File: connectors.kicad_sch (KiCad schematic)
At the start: 21 parts, among them J10 Conn_01x02, J11 Conn_01x02, J12 Conn_01x02, J13 Conn_01x02, J14 Conn_01x02, J15 Conn_01x02, J16 Conn_01x02, J17 Conn_01x02, J18 Conn_01x02, J19 Conn_01x02, J2 Conn_01x02, J20 Conn_01x02, J21 Conn_01x02, J22 Conn_01x02, J23 Conn_01x02, J24 Conn_01x02, J3 Conn_01x02, J5 Conn_01x02, J7 Conn_01x02, J8 Conn_01x02, J9 Conn_01x02

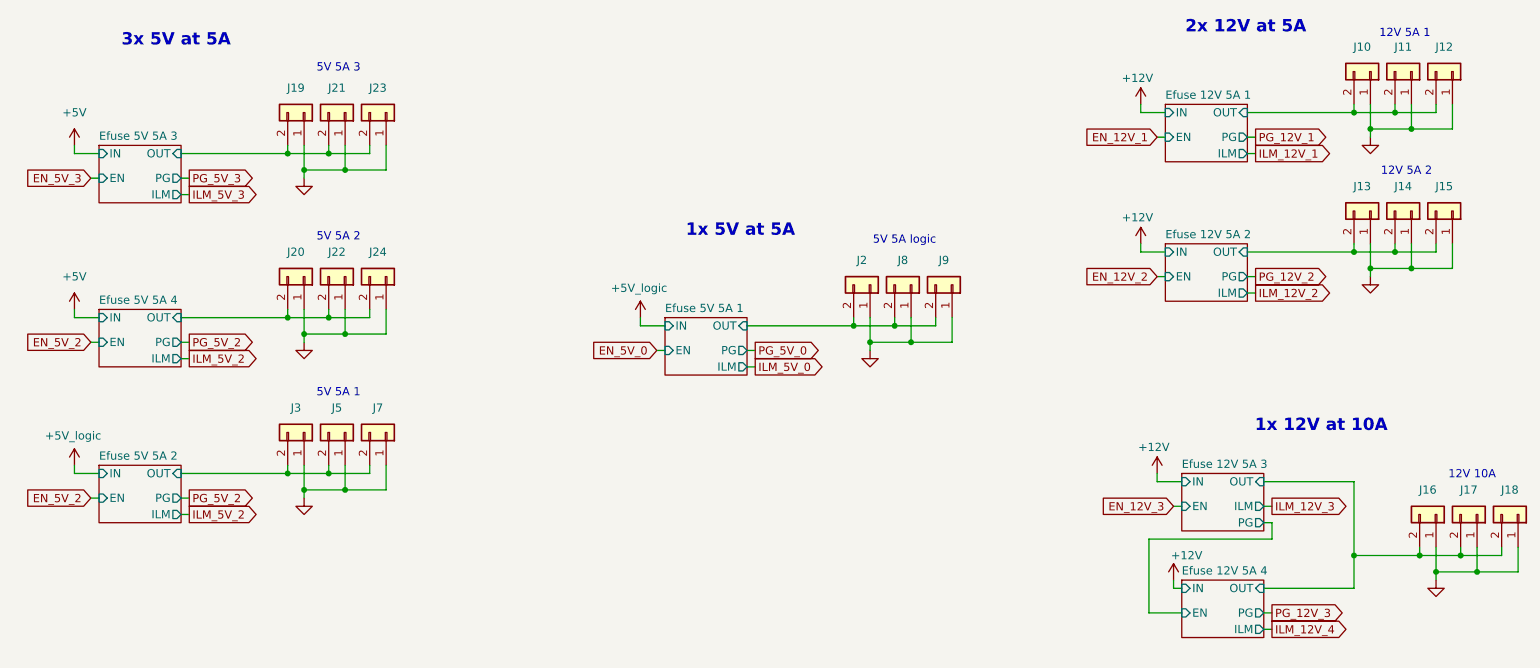
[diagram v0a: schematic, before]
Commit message: schem: removed 5V output
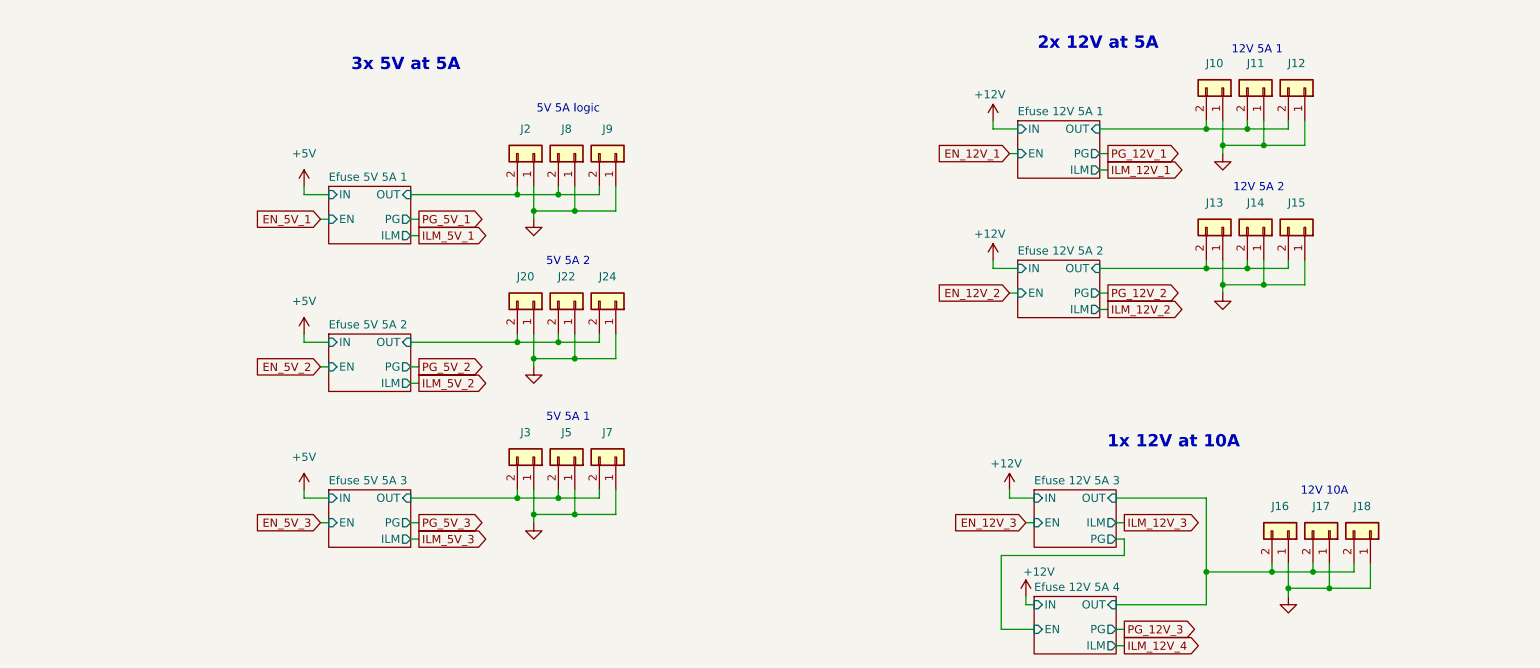
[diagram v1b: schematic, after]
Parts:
- removed J19, J21, J23: Conn_01x02, Connector_JST:JST_XH_B2B-XH-A_1x02_P2.50mm_Vertical, symbol Connector_Generic:Conn_01x02
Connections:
- net Efuse 5V 5A 4/OUT is gone; now on net Efuse 5V 5A 2/OUT: J20.2 (Pin_2), J22.2 (Pin_2), J24.2 (Pin_2)
- net Efuse 5V 5A 2/OUT: no longer J3.2 (Pin_2), J5.2 (Pin_2), J7.2 (Pin_2)
- net Efuse 5V 5A 3/OUT: now also J3.2 (Pin_2), J5.2 (Pin_2), J7.2 (Pin_2)
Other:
- removed sheet Efuse 5V 5A 4
- note removed: "1x 5V at 5A"
- note removed: "5V 5A 3"
- moved on the sheet: J10, J11, J12, J13, J14, J15, J16, J17, J18, J2, J20, J22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

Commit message: schem: run and fix ERC
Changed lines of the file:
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@@
+	)
+	(junction
+		(at 181.61 144.78)
+		(diameter 0)
+		(color 0 0 0 0)
 	)
 	(junction
@@
 	(wire
 		(pts
+			(xy 180.34 144.78) (xy 181.61 144.78)
+		)
+		(stroke
+			(width 0)
+			(type default)
+		)
+	)
+	(wire
+		(pts
 			(xy 179.07 66.04) (xy 179.07 67.31)
 		)
@@
 	(wire
 		(pts
-			(xy 180.34 133.35) (xy 180.34 144.78)
+			(xy 181.61 133.35) (xy 181.61 144.78)
 		)
 		(stroke
@@
 	(wire
 		(pts
-			(xy 180.34 144.78) (xy 185.42 144.78)
+			(xy 181.61 144.78) (xy 185.42 144.78)
 		)
 		(stroke
@@
 	(wire
 		(pts
-			(xy 199.39 133.35) (xy 180.34 133.35)
+			(xy 199.39 133.35) (xy 181.61 133.35)
 		)
 		(stroke
@@
 		)
 	)
+	(global_label "PG_12V_3"
+		(shape input)
+		(at 180.34 144.78 180)
+		(fields_autoplaced yes)
+		(effects
+			(font
+				(size 1.27 1.27)
+			)
+			(justify right)
+		)
+		(property "Intersheetrefs" "${INTERSHEET_REFS}"
+			(at 168.1625 144.78 0)
+			(effects
+				(font
+					(size 1.27 1.27)
+				)
+				(justify right)
+				(hide yes)
+			)
+		)
+	)
 	(global_label "ILM_5V_3"
 		(shape output)
@@
 		)
 	)
-	(global_label "PG_12V_3"
+	(global_label "PG_12V_4"
 		(shape output)
 		(at 199.39 144.78 0)

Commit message: schem: add sheet title
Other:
- company: (none) -> Valrobotik
- title: (none) -> Carte alim CDF 1
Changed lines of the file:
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@@
 	(generator_version "9.0")
 	(paper "A4")
+	(title_block
+		(title "Carte alim CDF 1")
+		(date "2026-01-15")
+		(rev "01")
+		(company "Valrobotik")
+	)
 	(text "5V 5A 1"
 		(exclude_from_sim no)

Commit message: schem: renumber
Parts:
- renumbered J5 to J10, J9 to J11, J24 to J12, J7 to J13, J10 to J14, J13 to J15, J11 to J16, J14 to J17, J16 to J18, J12 to J19, J15 to J20, J17 to J21, J18 to J22, J2 to J5, J20 to J6, J3 to J7, J22 to J9
